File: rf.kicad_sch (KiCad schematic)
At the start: 13 parts, among them J12 GPS_ANT, Q8 2N7002, SW4 GPS_RST, U11 L80-R

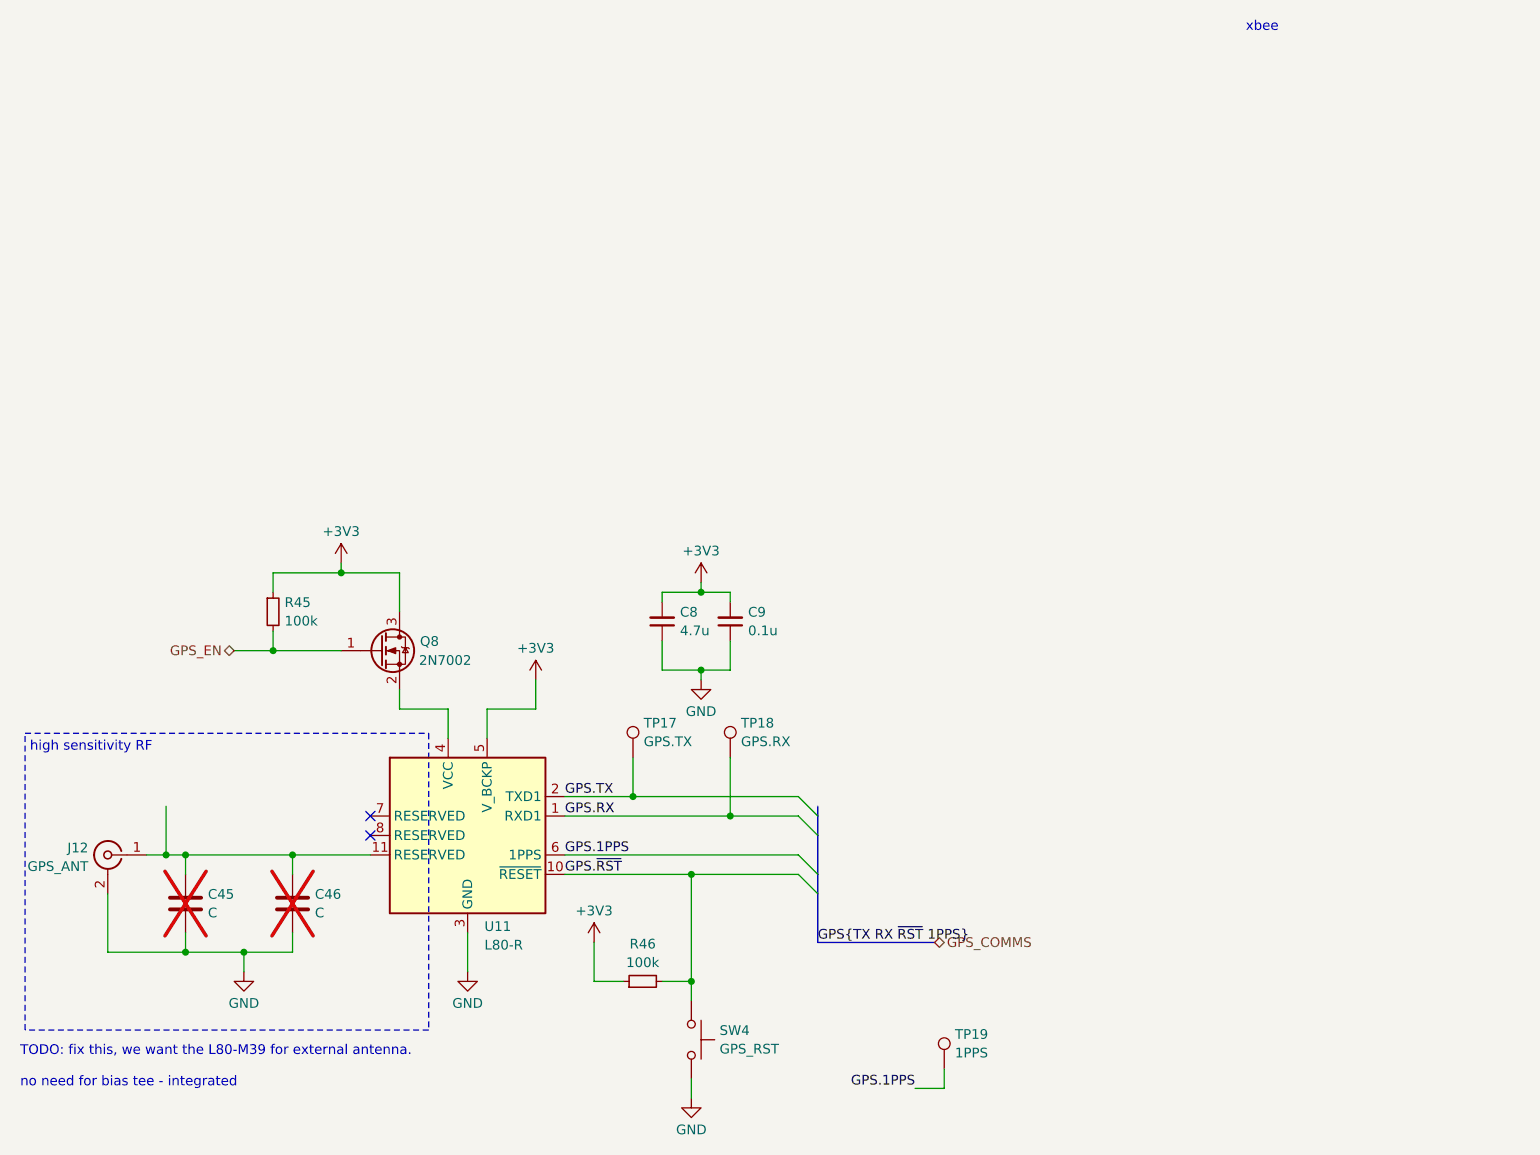
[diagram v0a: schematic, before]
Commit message: minor schematic reorg
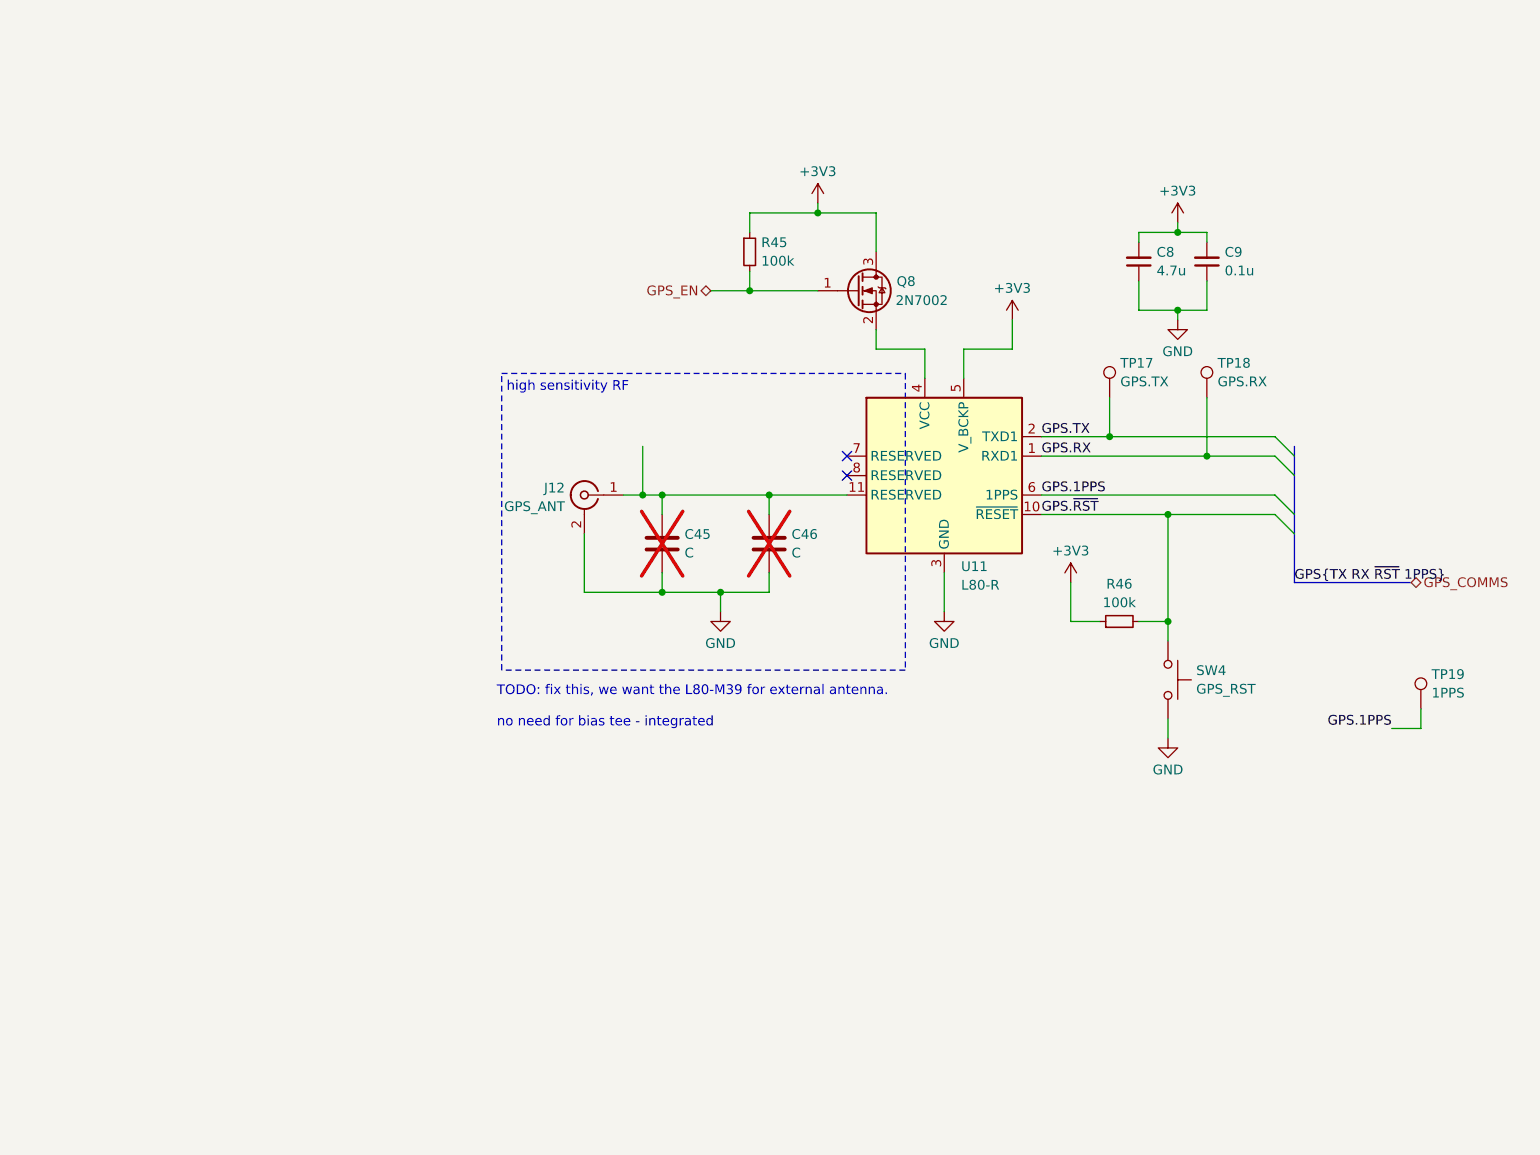
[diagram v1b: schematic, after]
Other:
- note removed: "xbee"
- moved on the sheet: C45, C46, C8, C9, J12, Q8, R45, R46, SW4, TP17, TP18, TP19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

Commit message: fix uart gps
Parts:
- added Q9: DMG2301L, Package_TO_SOT_SMD:SOT-23, symbol Transistor_FET:DMG2301L
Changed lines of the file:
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@@
+    )
+  )
+  (symbol (lib_id "Transistor_FET:DMG2301L") (at 143.51 54.61 0) (unit 1)
+    (in_bom yes) (on_board yes) (dnp no) (fields_autoplaced)
+    (property "Reference" "Q9" (at 148.717 53.3979 0)
+      (effects (font (size 1.27 1.27)) (justify left))
+    )
+    (property "Value" "DMG2301L" (at 148.717 55.8221 0)
+      (effects (font (size 1.27 1.27)) (justify left))
+    )
+    (property "Footprint" "Package_TO_SOT_SMD:SOT-23" (at 148.59 56.515 0)
+      (effects (font (size 1.27 1.27) italic) (justify left) hide)
+    )
+    (property "Datasheet" "https://www.diodes.com/assets/Datasheets/DMG2301L.pdf" (at 143.51 54.61 0)
+      (effects (font (size 1.27 1.27)) (justify left) hide)
+    )
+    (pin "1")
+    (pin "2")
+    (pin "3")
+    (instances
+      (project "telem3"
+        (path "/bc28f926-3cf9-4560-a9ac-15cb5699adb1/6dd8ae93-a1e2-4444-9ffc-657cfa4c8ecd"
+          (reference "Q9") (unit 1)
+        )
+      )
     )
   )
